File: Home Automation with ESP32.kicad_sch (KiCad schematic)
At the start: 20 parts, among them J1 Conn_01x04_Pin, J1 PR13-5V-450-1C, J2 Screw_Terminal_01x04, J3 Screw_Terminal_01x03, K1 RAYEX-L90AS, Q1 S8050, Q2 S8050, SW1 SW_Push, SW2 SW_Push, U1 ESP32-WROOM-32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

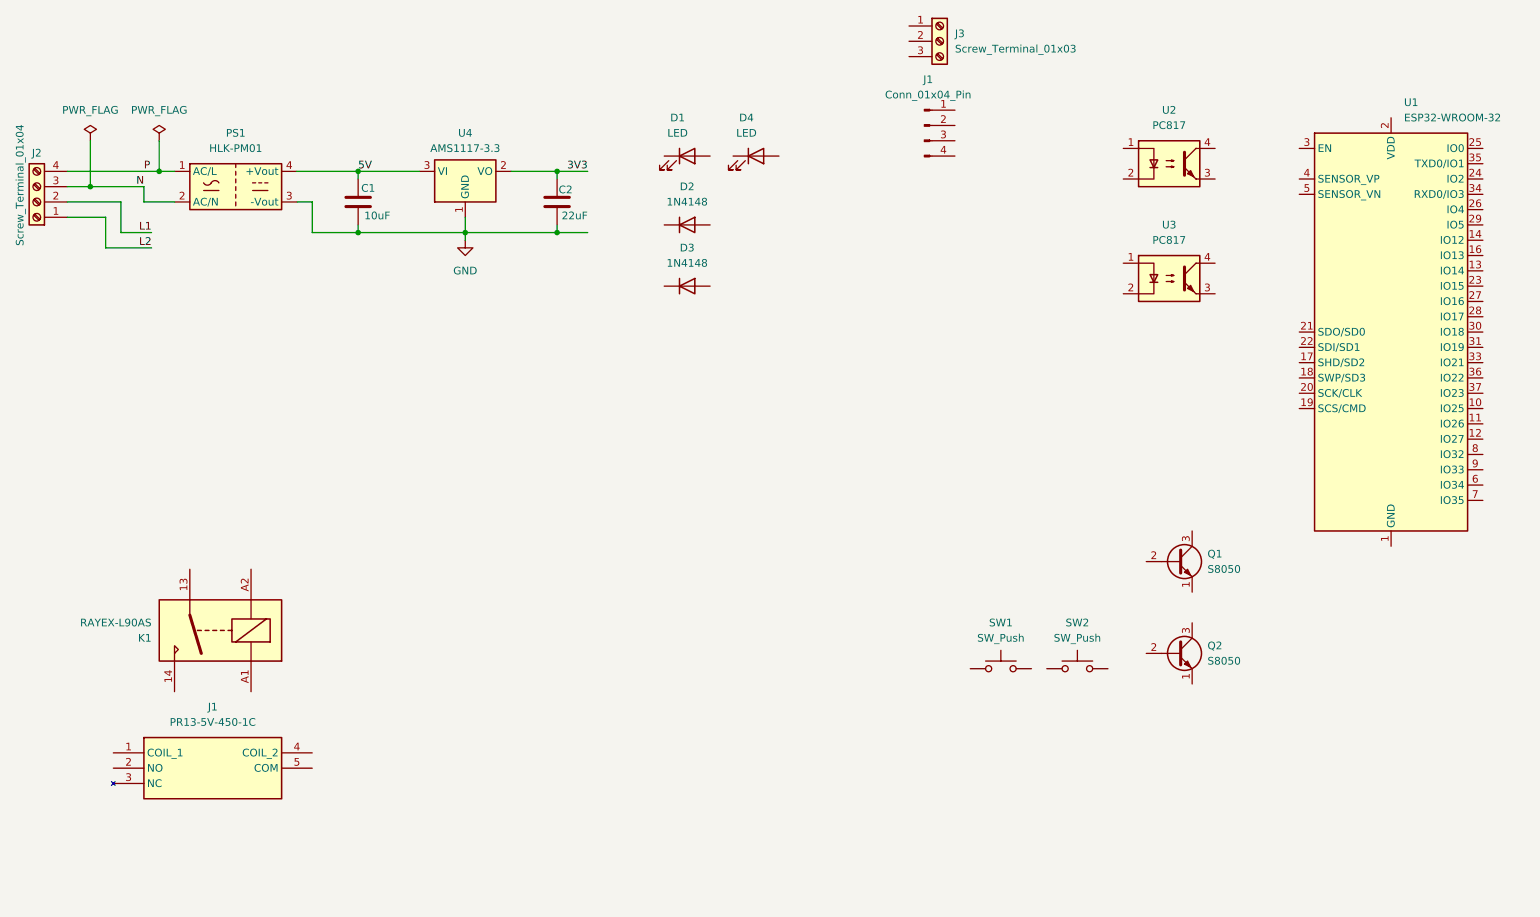
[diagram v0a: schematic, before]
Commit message: Placed Resistors in Schematic
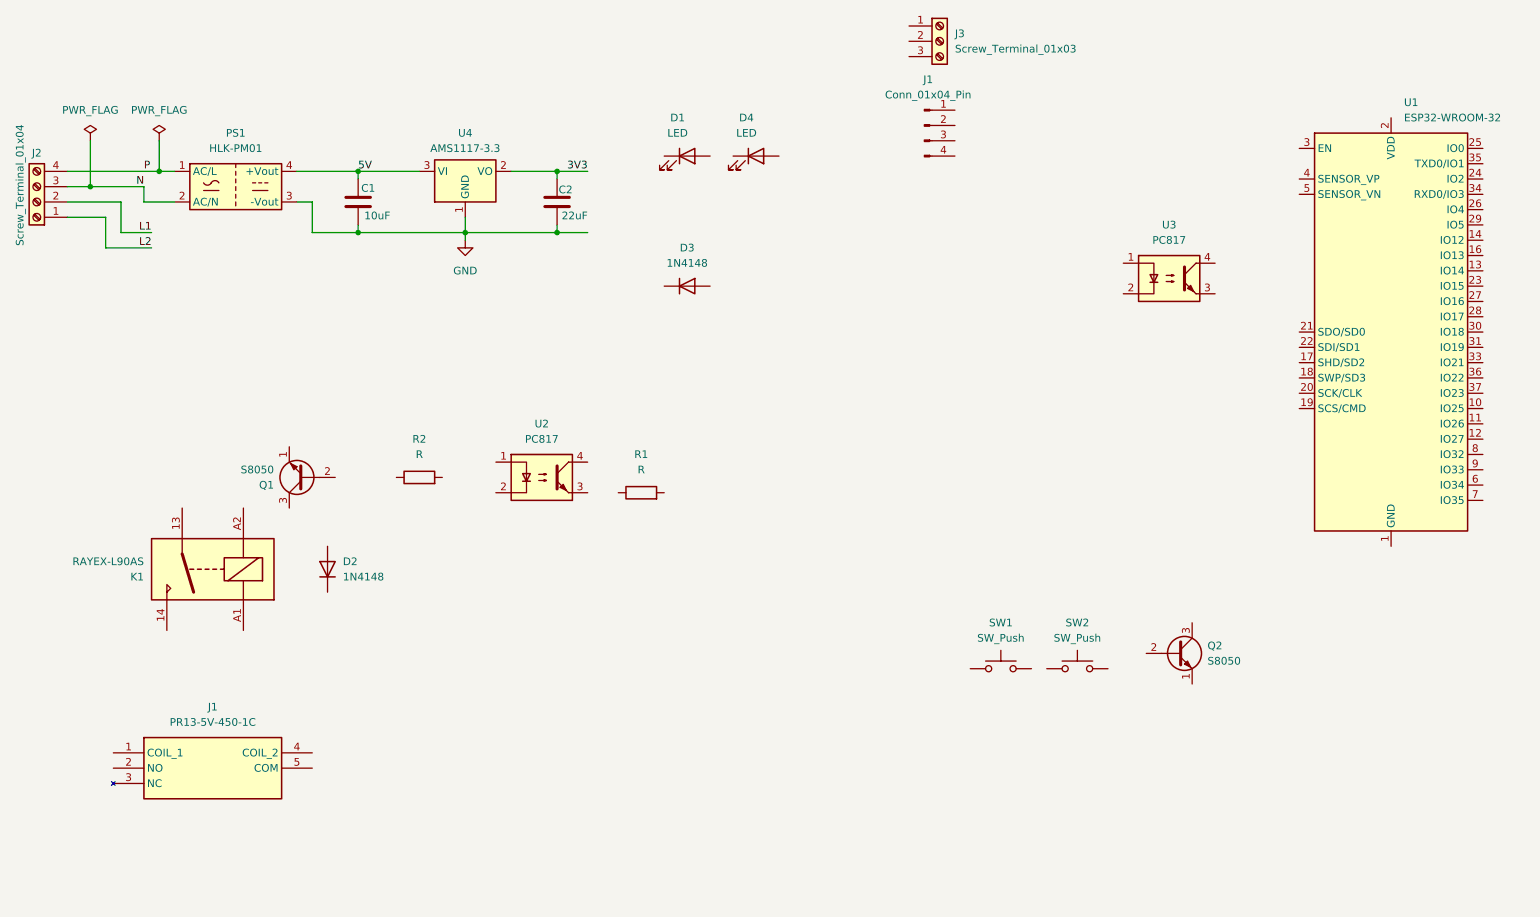
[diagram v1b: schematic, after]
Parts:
- added R1, R2: R, symbol Device:R
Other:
- moved on the sheet: D2, K1, Q1, U2
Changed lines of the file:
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@@
 	(symbol
 		(lib_id "Transistor_BJT:S8050")
-		(at 210.82 106.68 0)
-		(unit 1)
-		(exclude_from_sim no)
-		(in_bom yes)
-		(on_board yes)
-		(dnp no)
-		(fields_autoplaced yes)
+		(at 66.04 92.71 180)
+		(unit 1)
+		(exclude_from_sim no)
+		(in_bom yes)
+		(on_board yes)
+		(dnp no)
 		(property "Reference" "Q1"
-			(at 215.9 105.4099 0)
+			(at 60.96 93.9801 0)
 			(effects
 				(font
@@
 		)
 		(property "Value" "S8050"
-			(at 215.9 107.9499 0)
+			(at 60.96 91.4401 0)
 			(effects
 				(font
@@
 		)
 		(property "Footprint" "Package_TO_SOT_THT:TO-92_Inline"
-			(at 215.9 108.585 0)
+			(at 60.96 90.805 0)
 			(effects
 				(font
@@
 		)
 		(property "Datasheet" "http://www.unisonic.com.tw/datasheet/S8050.pdf"
-			(at 210.82 106.68 0)
+			(at 66.04 92.71 0)
 			(effects
 				(font
@@
 		)
 		(property "Description" "0.7A Ic, 20V Vce, Low Voltage High Current NPN Transistor, TO-92"
-			(at 210.82 106.68 0)
+			(at 66.04 92.71 0)
 			(effects
 				(font
@@
 	(symbol
 		(lib_id "Relay:RAYEX-L90AS")
-		(at 52.07 118.11 180)
+		(at 50.8 107.95 180)
 		(unit 1)
 		(exclude_from_sim no)
@@
 		(dnp no)
 		(property "Reference" "K1"
-			(at 40.64 119.3801 0)
+			(at 39.37 109.2201 0)
 			(effects
 				(font
@@
 		)
 		(property "Value" "RAYEX-L90AS"
-			(at 40.64 116.8401 0)
+			(at 39.37 106.6801 0)
 			(effects
 				(font
@@
 		)
 		(property "Footprint" "Relay_THT:Relay_SPST_RAYEX-L90AS"
-			(at 40.64 116.84 0)
+			(at 39.37 106.68 0)
 			(effects
 				(font
@@
 		)
 		(property "Datasheet" "https://a3.sofastcdn.com/attachment/7jioKBjnRiiSrjrjknRiwS77gwbf3zmp/L90-SERIES.pdf"
-			(at 34.29 114.3 0)
+			(at 33.02 104.14 0)
 			(effects
 				(font
@@
 		)
 		(property "Description" "Power relay, Without Common Terminal between coil terminals, NO, SPST, 30A"
-			(at 52.07 118.11 0)
+			(at 50.8 107.95 0)
 			(effects
 				(font
@@
 	(symbol
 		(lib_id "Isolator:PC817")
-		(at 209.55 40.64 0)
+		(at 105.41 92.71 0)
 		(unit 1)
 		(exclude_from_sim no)
@@
 		(fields_autoplaced yes)
 		(property "Reference" "U2"
-			(at 209.55 31.75 0)
+			(at 105.41 83.82 0)
 			(effects
 				(font
@@
 		)
 		(property "Value" "PC817"
-			(at 209.55 34.29 0)
+			(at 105.41 86.36 0)
 			(effects
 				(font
@@
 		)
 		(property "Footprint" "Package_DIP:DIP-4_W7.62mm"
-			(at 204.47 45.72 0)
+			(at 100.33 97.79 0)
 			(effects
 				(font
@@
 		)
 		(property "Datasheet" "http://www.soselectronic.cz/a_info/resource/d/pc817.pdf"
-			(at 209.55 40.64 0)
+			(at 105.41 92.71 0)
 			(effects
 				(font
@@
 		)
 		(property "Description" "DC Optocoupler, Vce 35V, CTR 50-300%, DIP-4"
-			(at 209.55 40.64 0)
+			(at 105.41 92.71 0)
 			(effects
 				(font
@@
 	)
 	(symbol
+		(lib_id "Device:R")
+		(at 85.09 92.71 90)
+		(unit 1)
+		(exclude_from_sim no)
+		(in_bom yes)
+		(on_board yes)
+		(dnp no)
+		(fields_autoplaced yes)
+		(property "Reference" "R2"
+			(at 85.09 86.36 90)
+			(effects
+				(font
+					(size 1.27 1.27)
+				)
+			)
+		)
+		(property "Value" "R"
+			(at 85.09 88.9 90)
+			(effects
+				(font
+					(size 1.27 1.27)
+				)
+			)
+		)
+		(property "Footprint" ""
+			(at 85.09 94.488 90)
+			(effects
+				(font
+					(size 1.27 1.27)
+				)
+				(hide yes)
+			)
+		)
+		(property "Datasheet" "~"
+			(at 85.09 92.71 0)
+			(effects
+				(font
+					(size 1.27 1.27)
+				)
+				(hide yes)
+			)
+		)
+		(property "Description" "Resistor"
+			(at 85.09 92.71 0)
+			(effects
+				(font
+					(size 1.27 1.27)
+				)
+				(hide yes)
+			)
+		)
+		(pin "2"
+		)
+		(pin "1"
+		)
+		(instances
+			(project "Home Automation with ESP32"
+				(path "/7438dd54-9f08-4599-aef6-4a86e3e5147b"
+					(reference "R2")
+					(unit 1)
+				)
+			)
+		)
+	)
+	(symbol
 		(lib_id "Diode:1N4148")
-		(at 129.54 50.8 0)
+		(at 69.85 107.95 90)
 		(unit 1)
 		(exclude_from_sim no)
@@
 		(fields_autoplaced yes)
 		(property "Reference" "D2"
-			(at 129.54 44.45 0)
-			(effects
-				(font
-					(size 1.27 1.27)
-				)
+			(at 72.39 106.6799 90)
+			(effects
+				(font
+					(size 1.27 1.27)
+				)
+				(justify right)
 			)
 		)
 		(property "Value" "1N4148"
-			(at 129.54 46.99 0)
-			(effects
-				(font
-					(size 1.27 1.27)
-				)
+			(at 72.39 109.2199 90)
+			(effects
+				(font
+					(size 1.27 1.27)
+				)
+				(justify right)
 			)
 		)
 		(property "Footprint" "Diode_THT:D_DO-35_SOD27_P7.62mm_Horizontal"
-			(at 129.54 50.8 0)
+			(at 69.85 107.95 0)
 			(effects
 				(font
@@
 		)
 		(property "Datasheet" "https://assets.nexperia.com/documents/data-sheet/1N4148_1N4448.pdf"
-			(at 129.54 50.8 0)
+			(at 69.85 107.95 0)
 			(effects
 				(font
@@
 		)
 		(property "Description" "100V 0.15A standard switching diode, DO-35"
-			(at 129.54 50.8 0)
+			(at 69.85 107.95 0)
 			(effects
 				(font
@@
 		)
 		(property "Sim.Device" "D"
-			(at 129.54 50.8 0)
+			(at 69.85 107.95 0)
 			(effects
 				(font
@@
 		)
 		(property "Sim.Pins" "1=K 2=A"
-			(at 129.54 50.8 0)
+			(at 69.85 107.95 0)
 			(effects
 				(font
@@
 					(unit 1)
 				)
+			)
+		)
+	)
+	(symbol
+		(lib_id "Device:R")
+		(at 121.92 95.25 90)
+		(unit 1)
+		(exclude_from_sim no)
+		(in_bom yes)
+		(on_board yes)
+		(dnp no)
+		(fields_autoplaced yes)
+		(property "Reference" "R1"
+			(at 121.92 88.9 90)
+			(effects
+				(font
+					(size 1.27 1.27)
+				)
+			)
+		)
+		(property "Value" "R"
+			(at 121.92 91.44 90)
+			(effects
+				(font
+					(size 1.27 1.27)
+				)
+			)
+		)
+		(property "Footprint" ""
+			(at 121.92 97.028 90)
+			(effects
+				(font
+					(size 1.27 1.27)
+				)
+				(hide yes)
+			)
+		)
+		(property "Datasheet" "~"
+			(at 121.92 95.25 0)
+			(effects
+				(font
+					(size 1.27 1.27)
+				)
+				(hide yes)
+			)
+		)
+		(property "Description" "Resistor"
+			(at 121.92 95.25 0)
+			(effects
+				(font
+					(size 1.27 1.27)
+				)
+				(hide yes)
+			)
+		)
+		(pin "2"
+		)
+		(pin "1"
+		)
+		(instances
+			(project ""
+				(path "/7438dd54-9f08-4599-aef6-4a86e3e5147b"
+					(reference "R1")
+					(unit 1)
+				)

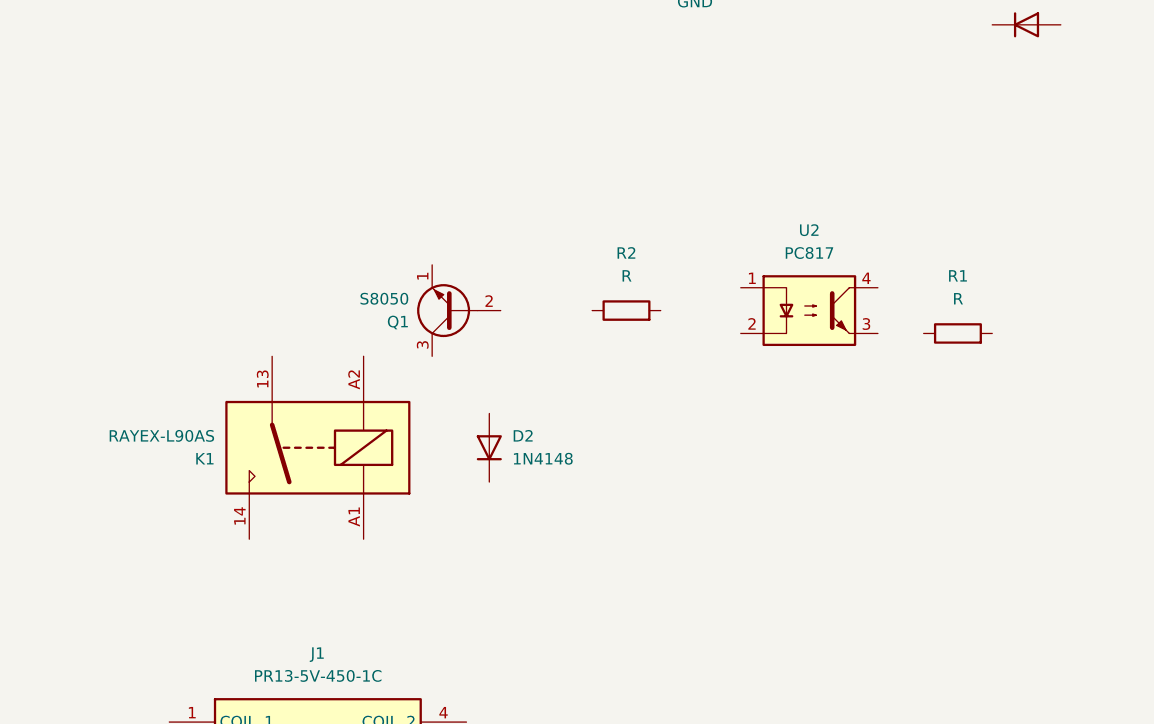
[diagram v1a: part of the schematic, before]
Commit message: Placed Wires for Relay-1 in Schematic
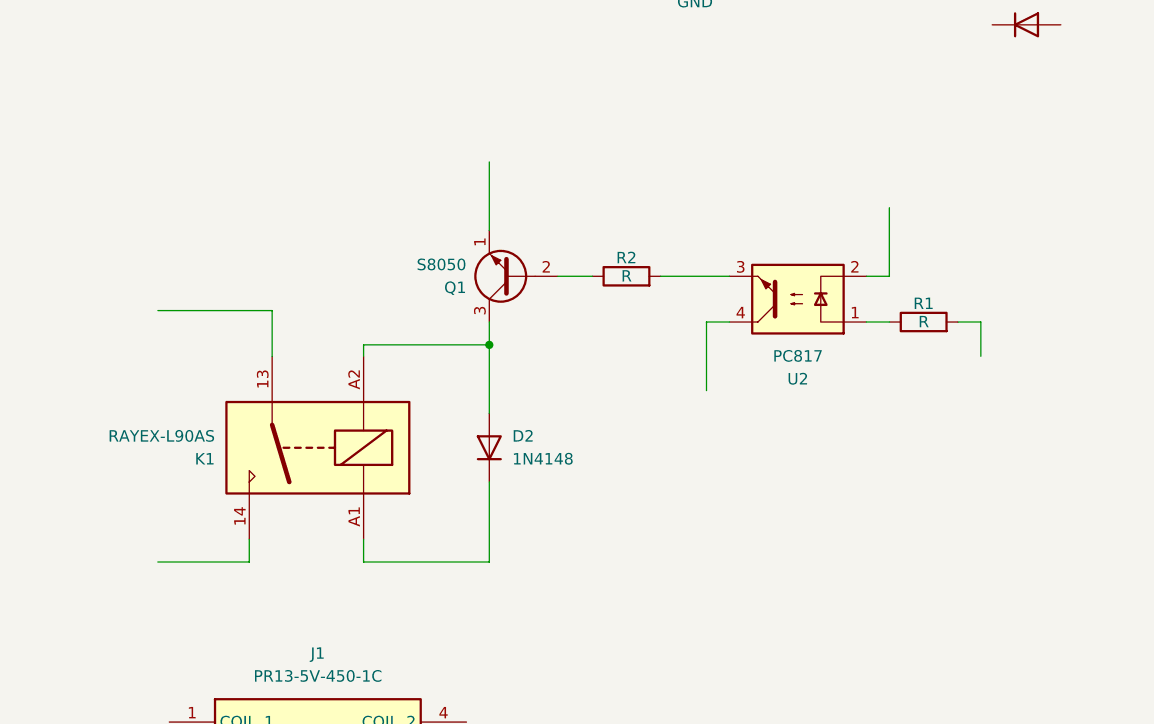
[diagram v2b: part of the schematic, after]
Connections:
- net at Q1.2 (B): now also R2.1
- net at Q1.3 (C): now also D2.2 (A), K1.A2
- net at K1.A1: now also D2.1 (K)
- net at U2.1: now also R1.1
- net at U2.3: now also R2.2
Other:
- moved on the sheet: Q1, R1, R2, U2

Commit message: Placed GND in Schematic
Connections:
- net GND: now also Q1.1 (E), U2.2, U2.4
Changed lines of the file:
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@@
+	)
+	(symbol
+		(lib_id "power:GND")
+		(at 114.3 81.28 180)
+		(unit 1)
+		(exclude_from_sim no)
+		(in_bom yes)
+		(on_board yes)
+		(dnp no)
+		(fields_autoplaced yes)
+		(property "Reference" "#PWR03"
+			(at 114.3 74.93 0)
+			(effects
+				(font
+					(size 1.27 1.27)
+				)
+				(hide yes)
+			)
+		)
+		(property "Value" "GND"
+			(at 114.3 76.2 0)
+			(effects
+				(font
+					(size 1.27 1.27)
+				)
+			)
+		)
+		(property "Footprint" ""
+			(at 114.3 81.28 0)
+			(effects
+				(font
+					(size 1.27 1.27)
+				)
+				(hide yes)
+			)
+		)
+		(property "Datasheet" ""
+			(at 114.3 81.28 0)
+			(effects
+				(font
+					(size 1.27 1.27)
+				)
+				(hide yes)
+			)
+		)
+		(property "Description" "Power symbol creates a global label with name \"GND\" , ground"
+			(at 114.3 81.28 0)
+			(effects
+				(font
+					(size 1.27 1.27)
+				)
+				(hide yes)
+			)
+		)
+		(pin "1"
+		)
+		(instances
+			(project "Home Automation with ESP32"
+				(path "/7438dd54-9f08-4599-aef6-4a86e3e5147b"
+					(reference "#PWR03")
+					(unit 1)
+				)
+			)
+		)
 	)
 	(symbol
@@
 	)
 	(symbol
+		(lib_id "power:GND")
+		(at 93.98 101.6 0)
+		(unit 1)
+		(exclude_from_sim no)
+		(in_bom yes)
+		(on_board yes)
+		(dnp no)
+		(fields_autoplaced yes)
+		(property "Reference" "#PWR02"
+			(at 93.98 107.95 0)
+			(effects
+				(font
+					(size 1.27 1.27)
+				)
+				(hide yes)
+			)
+		)
+		(property "Value" "GND"
+			(at 93.98 106.68 0)
+			(effects
+				(font
+					(size 1.27 1.27)
+				)
+			)
+		)
+		(property "Footprint" ""
+			(at 93.98 101.6 0)
+			(effects
+				(font
+					(size 1.27 1.27)
+				)
+				(hide yes)
+			)
+		)
+		(property "Datasheet" ""
+			(at 93.98 101.6 0)
+			(effects
+				(font
+					(size 1.27 1.27)
+				)
+				(hide yes)
+			)
+		)
+		(property "Description" "Power symbol creates a global label with name \"GND\" , ground"
+			(at 93.98 101.6 0)
+			(effects
+				(font
+					(size 1.27 1.27)
+				)
+				(hide yes)
+			)
+		)
+		(pin "1"
+		)
+		(instances
+			(project "Home Automation with ESP32"
+				(path "/7438dd54-9f08-4599-aef6-4a86e3e5147b"
+					(reference "#PWR02")
+					(unit 1)
+				)
+			)
+		)
+	)
+	(symbol
 		(lib_id "Device:R")
 		(at 85.09 88.9 90)
@@
 					(unit 1)
 				)
+			)
+		)
+	)
+	(symbol
+		(lib_id "power:GND")
+		(at 69.85 76.2 180)
+		(unit 1)
+		(exclude_from_sim no)
+		(in_bom yes)
+		(on_board yes)
+		(dnp no)
+		(fields_autoplaced yes)
+		(property "Reference" "#PWR04"
+			(at 69.85 69.85 0)
+			(effects
+				(font
+					(size 1.27 1.27)
+				)
+				(hide yes)
+			)
+		)
+		(property "Value" "GND"
+			(at 69.85 71.12 0)
+			(effects
+				(font
+					(size 1.27 1.27)
+				)
+			)
+		)
+		(property "Footprint" ""
+			(at 69.85 76.2 0)
+			(effects
+				(font
+					(size 1.27 1.27)
+				)
+				(hide yes)
+			)
+		)
+		(property "Datasheet" ""
+			(at 69.85 76.2 0)
+			(effects
+				(font
+					(size 1.27 1.27)
+				)
+				(hide yes)
+			)
+		)
+		(property "Description" "Power symbol creates a global label with name \"GND\" , ground"
+			(at 69.85 76.2 0)
+			(effects
+				(font
+					(size 1.27 1.27)
+				)
+				(hide yes)
+			)
+		)
+		(pin "1"
+		)
+		(instances
+			(project "Home Automation with ESP32"
+				(path "/7438dd54-9f08-4599-aef6-4a86e3e5147b"
+					(reference "#PWR04")
+					(unit 1)
+				)

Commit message: Placed Net Labels in Relay-1 in Schematic
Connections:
- net 5V: now also D2.1 (K), K1.A1
- net L1: now also K1.13
- net P: now also K1.14
- net R1: now reaches R1.2
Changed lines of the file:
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@@
+		)
+	)
+	(label "5V"
+		(at 62.23 120.65 0)
+		(effects
+			(font
+				(size 1.27 1.27)
+			)
+			(justify left bottom)
 		)
 	)
@@
 		(effects
 			(font
+				(size 1.27 1.27)
+			)
+			(justify left bottom)
+		)
+	)
+	(label "R1"
+		(at 124.46 97.79 180)
+		(effects
+			(font
+				(size 1.27 1.27)
+			)
+			(justify right bottom)
+		)
+	)
+	(label "L1"
+		(at 33.02 92.71 0)
+		(effects
+			(font
+				(size 1.27 1.27)
+			)
+			(justify left bottom)
+		)
+	)
+	(label "P"
+		(at 33.02 120.65 0)
+		(effects
+			(font
